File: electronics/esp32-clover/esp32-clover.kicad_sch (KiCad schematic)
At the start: 62 parts

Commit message: added pcb layout and imgs folder
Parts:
- removed J?: FTDI_CONN, symbol Connector:Conn_01x03_Male
- removed JP? (x2): SJ_B, symbol Jumper:SolderJumper_2_Bridged
- added D6: LED, LED_SMD:LED_0603_1608Metric, symbol Device:LED
- added J3: Conn_01x08_Male, Connector_PinHeader_2.54mm:PinHeader_1x08_P2.54mm_Vertical, symbol Connector:Conn_01x08_Male
- added J5: Conn_01x10_Male, Connector_PinHeader_2.54mm:PinHeader_1x10_P2.54mm_Vertical, symbol Connector:Conn_01x10_Male
- added R19: 10K, Resistor_SMD:R_0603_1608Metric, symbol Device:R
- added R20: 470, Resistor_SMD:R_0603_1608Metric, symbol Device:R
- added SW3: PROG_BTN, MCIPTG23K-V:MCIPTG23K-V, symbol MCIPTG23K-V:MCIPTG23K-V
- C1, C10, C11, C12, C13, C14, C15, C16, C17, C2, C3, C4, C5, C6, C7, C8, C9: renamed from C?; footprint Capacitor_SMD:C_0805_2012Metric -> Capacitor_SMD:C_0603_1608Metric
- D1, D3, D4, D5: renamed from D?; footprint LED_SMD:LED_0805_2012Metric -> LED_SMD:LED_0603_1608Metric
- J1: renamed from J?; footprint GCT_USB4055-30-A -> USB4055-30-A:USB4055-30-A
- J2: renamed from J?; footprint JST_S2B-PH-K-S(LF)(SN) -> S2B-PH-K-S_LF__SN:S2B-PH-K-S_LF__SN
- J4: renamed from J?; footprint (none) -> jtag:3221-10-0100-00
- JP1, JP2, JP3, JP4: renamed from JP?; footprint (none) -> Jumper:SolderJumper-2_P1.3mm_Bridged_Pad1.0x1.5mm
- LS1: renamed from LS?; footprint SPKR_PKMCS0909E4000-R1 -> PKMCS0909E4000-R1:PKMCS0909E4000-R1
- R1, R10, R11, R12, R13, R14, R15, R16, R17, R18, R2, R3, R4, R5, R6, R7, R8, R9: renamed from R?; footprint Resistor_SMD:R_0805_2012Metric -> Resistor_SMD:R_0603_1608Metric
- SW1, SW2: renamed from SW?; footprint MCIPTG23K-V_MTC -> MCIPTG23K-V:MCIPTG23K-V
- U2: renamed from U?; footprint Package_DFN_QFN:SiliconLabs_QFN-20-1EP_3x3mm_P0.5mm -> Package_DFN_QFN:SiliconLabs_QFN-20-1EP_3x3mm_P0.5mm_EP1.8x1.8mm
- U4: renamed from U?; footprint XCVR_ESP32-WROOM-32E_(16MB) -> ESP32:ESP32-WROOM-32E__16MB
- U5: renamed from U?; footprint (none) -> Package_SO:TSSOP-16_4.4x5mm_P0.65mm
- U6: renamed from U?; footprint SOP50P490X110-10N -> ADC124S101CIMM:ADC124S101CIMM
- U7: renamed from U?; footprint SOT95P280X145-6N -> DAC5571IDBVR:SOT95P280X145-6N
- Y1: renamed from Y?; footprint XTAL320X150X90 -> 32_768kHZ:ABS07AIG-32.768KHZ-T
- gave numbers to parts that had none: 4
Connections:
- net +3.3V: now also LS1.1, R18.2, R19.2
- net ADC_IN1: now also J3.2 (Pin_2)
- net ADC_IN3: now also J5.3 (Pin_3)
- net DAC_VOUT: now also J3.1 (Pin_1)
- net GND: now also D6.1 (K), J5.2 (Pin_2), SW3.4, SW3.5
- net GPIO17: now also J5.4 (Pin_4)
- net GPIO21/TCA9534_INT: now also J5.8 (Pin_8)
- net GPIO27/PIEZO: now also R17.2
- net I2C_SCL: now also J3.5 (Pin_5)
- net I2C_SDA: now also J3.6 (Pin_6)
- net SPI_MISO: now also J5.7 (Pin_7)
- net SPI_MOSI: now also J5.6 (Pin_6)
- net SPI_SCK: now also J5.5 (Pin_5)
- net TCA9534_P2: now also J3.4 (Pin_4)
- net TCA9534_P3: now also J3.3 (Pin_3)
- net UART_RX: now also J5.10 (Pin_10)
- net UART_RX1: now also J3.7 (Pin_7)
- net UART_TX: now also J5.9 (Pin_9)
- net UART_TX1: now also J3.8 (Pin_8)
- net VBAT: now also J5.1 (Pin_1)
- net VBUS: now also R20.2
- net GPI34 renamed GPI34/BTN
- net GPI34/BTN: now also R19.1, SW3.1
- new net: D6.2 (A), R20.1
- no-connect marks 27 -> 29
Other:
- note added: "TODO ADD UART TO EXTERNAL PINS"
- note removed: "UART Pins"

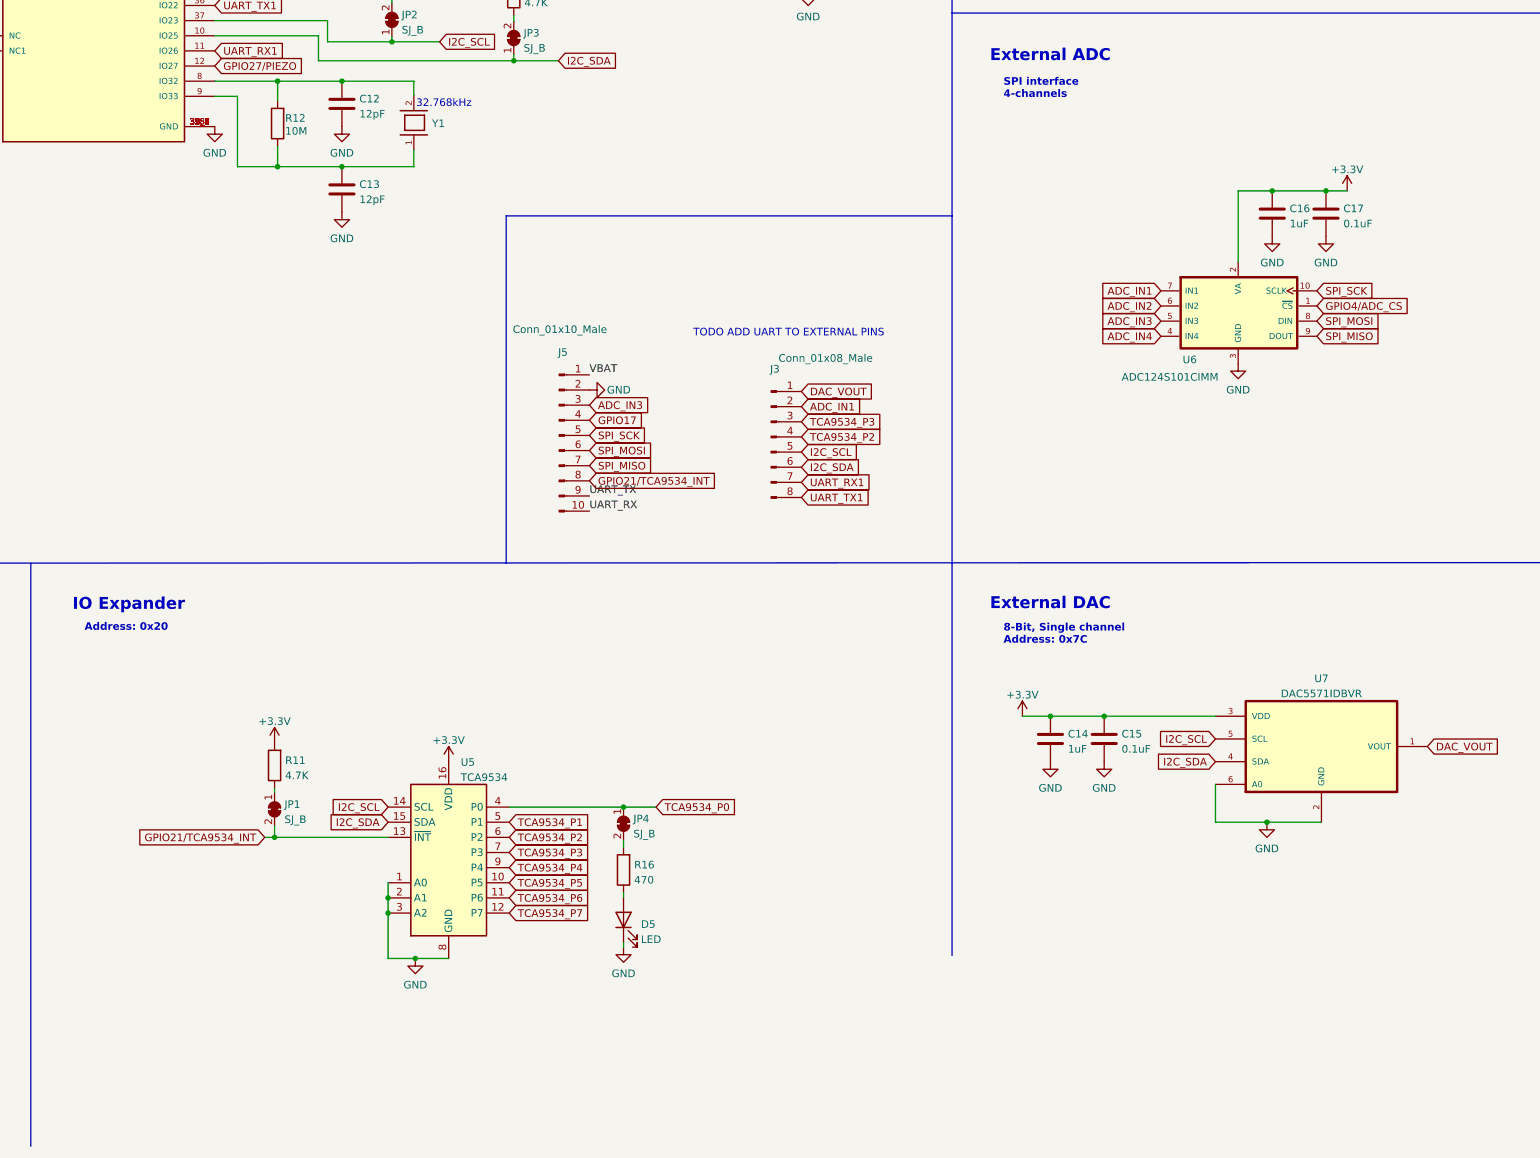
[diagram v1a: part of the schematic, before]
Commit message: added arduino variant pin definitions, still more to do
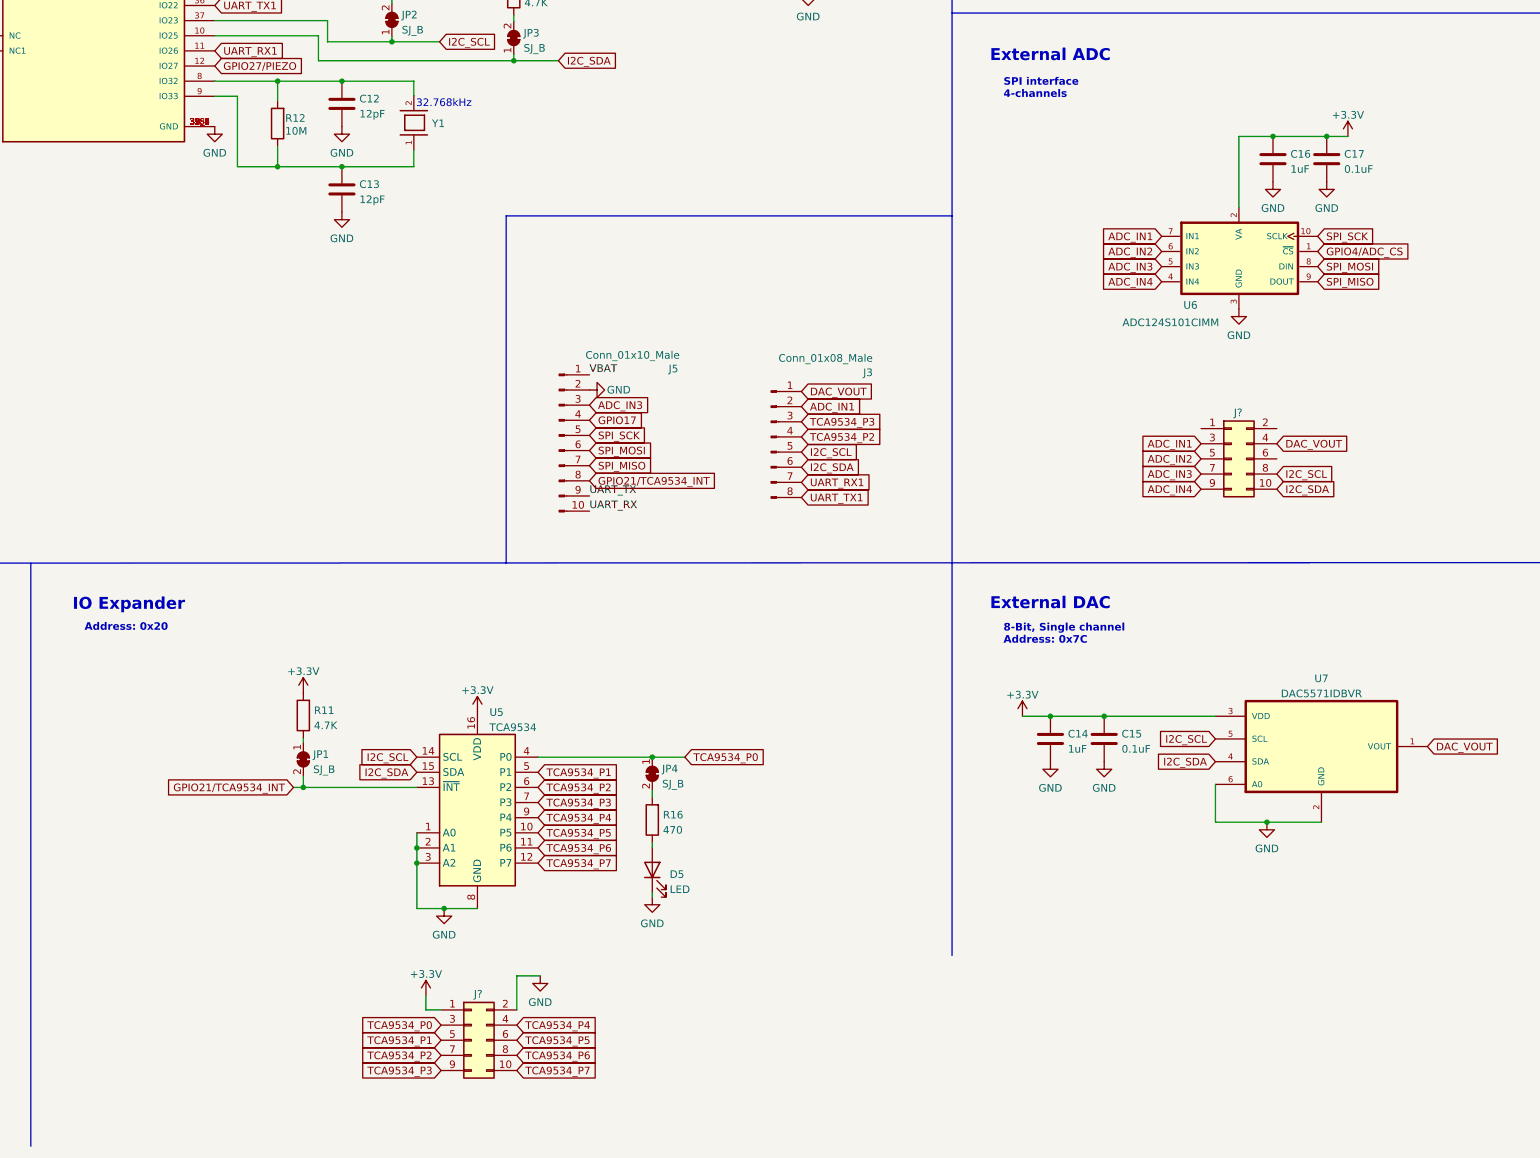
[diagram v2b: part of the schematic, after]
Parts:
- added J? (x2): Conn_02x05_Odd_Even, symbol Connector_Generic:Conn_02x05_Odd_Even
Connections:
- net +3.3V: now also J?.1 (Pin_1)
- net ADC_IN1: now also J?.3 (Pin_3)
- net ADC_IN2: now also J?.5 (Pin_5)
- net ADC_IN3: now also J?.7 (Pin_7)
- net ADC_IN4: now also J?.9 (Pin_9)
- net DAC_VOUT: now also J?.4 (Pin_4)
- net GND: now also J?.2 (Pin_2)
- net I2C_SCL: now also J?.8 (Pin_8)
- net I2C_SDA: now also J?.10 (Pin_10)
- net TCA9534_P0: now also J?.3 (Pin_3)
- net TCA9534_P1: now also J?.5 (Pin_5)
- net TCA9534_P2: now also J?.7 (Pin_7)
- net TCA9534_P3: now also J?.9 (Pin_9)
- net TCA9534_P4: now also J?.4 (Pin_4)
- net TCA9534_P5: now also J?.6 (Pin_6)
- net TCA9534_P6: now also J?.8 (Pin_8)
- net TCA9534_P7: now also J?.10 (Pin_10)
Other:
- note removed: "TODO ADD UART TO EXTERNAL PINS"
- moved on the sheet: C16, C17, D5, JP1, JP4, R11, R16, U5, U6

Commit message: update for v0.2
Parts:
- removed JP1, JP2, JP3, JP4: SJ_B, Jumper:SolderJumper-2_P1.3mm_Bridged_Pad1.0x1.5mm, symbol Jumper:SolderJumper_2_Bridged
- added C18: 4.7uF, Capacitor_SMD:C_0603_1608Metric, symbol Device:C
- added C19: TBD, Capacitor_SMD:C_0603_1608Metric, symbol Device:C
- added D7: D_Schottky, symbol Device:D_Schottky
- added Q2: MMDT3904, Package_TO_SOT_SMD:SOT-363_SC-70-6, symbol Transistor_BJT:MMDT3904
- added Q3: DMG2305UX-13, SOT91P240X110-3N, symbol DMG2305UX-13:DMG2305UX-13
- added R21: 1M, Resistor_SMD:R_0603_1608Metric, symbol Device:R
- added R22, R23: 10K, Resistor_SMD:R_0603_1608Metric, symbol Device:R
- added R24: 100K, Resistor_SMD:R_0603_1608Metric, symbol Device:R
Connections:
- net +3.3V: no longer U6.2 (VA)
- net ESP32_BOOT: now also Q2.3 (C2)
- net GND: now also C18.2, C19.2, R21.1, R24.1; no longer J1.S1 (SHIELD), J1.S2 (SHIELD), J1.S3 (SHIELD), J1.S4 (SHIELD), U6.3 (GND)
- net GPIO21/TCA9534_INT: now also R11.1
- net GPIO4/ADC_CS: no longer U6.1 (~{CS})
- net I2C_SCL: now also R14.1
- net I2C_SDA: now also R15.1
- net SPI_MISO: no longer U6.9 (DOUT)
- net SPI_MOSI: no longer U6.8 (DIN)
- net SPI_SCK: no longer U6.10 (SCLK)
- net TCA9534_P0: now also R16.2
- net USB_D+: now also J1.B6 (DP2)
- net USB_D-: now also J1.B7 (DN2)
- net VBUS: now also D7.2 (A), Q3.1, R24.2
- net at C12.1, R12.2, U4.8 (IO32): no longer Y1.2
- net at Q1.3 (C), R18.1: no longer LS1.2
- net ESP_EN: now reaches C9.1, R10.1, SW1.1, U4.3 (EN)
- net ESP_EN: now also Q2.6 (C1)
- net UART_DTR: now reaches U2.15 (~{CTS})
- net UART_DTR: now also Q2.4 (E2), R22.2
- net UART_RTS: now reaches U2.16 (~{RTS})
- net UART_RTS: now also Q2.1 (E1), R23.2
- net VBAT renamed +BATT
- net +BATT: now also Q3.3; no longer C5.1, U3.1 (VIN), U3.3 (EN)
- new net: C18.1, J1.S1 (SHIELD), J1.S2 (SHIELD), J1.S3 (SHIELD), J1.S4 (SHIELD), R21.2
- new net: Q2.2 (B1), R22.1
- new net: C19.1, C5.1, D7.1 (K), Q3.2, U3.1 (VIN), U3.3 (EN)
- new net: Q2.5 (B2), R23.1
- no-connect marks 29 -> 25
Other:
- note added: "3V3 Regulator"
- note added: "Battery Charger"
- note added: "Pwr"
- note added: "Single cell LiPo Charge Current: 400 mA Float voltage: 4.2 V Note: Max 500 mA with 2K resistor on PROG)"
- note added: "Upto 4 kHz (65 dB)"
- note added: "When VBUS (USB) is connected system is powered by USB."
- note removed: "Battery Charger & 3.3V Regulator"
- note removed: "Single cell LiPo Charge Current: 400 mA (Max 500 mA with 2K resistor on PROG) Float voltage: 4.2 V"
- note removed: "Upto 4 kHz (65 dB) Disable by cutting both jumpers"
- moved on the sheet: C1, C14, C15, C16, C17, C4, C5, C8, D1, D5, J2, J?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

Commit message: update for v2
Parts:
- removed C1, C18, C2, C4, C7: 4.7uF, Capacitor_SMD:C_0603_1608Metric, symbol Device:C
- removed C14, C16, C5, C8: 1uF, Capacitor_SMD:C_0603_1608Metric, symbol Device:C
- removed C15, C17, C3, C6: 0.1uF, Capacitor_SMD:C_0603_1608Metric, symbol Device:C
- removed C19: TBD, Capacitor_SMD:C_0603_1608Metric, symbol Device:C
- removed D1, D3, D4, D5, D6: LED, LED_SMD:LED_0603_1608Metric, symbol Device:LED
- removed D2: SP0503BAHT, Package_TO_SOT_SMD:SOT-143, symbol Power_Protection:SP0503BAHT
- removed D7: D_Schottky, symbol Device:D_Schottky
- removed J1: USB4055-30-A, USB4055-30-A:USB4055-30-A, symbol USB4055-30-A:USB4055-30-A
- removed J2: BATT_CONN, S2B-PH-K-S_LF__SN:S2B-PH-K-S_LF__SN, symbol S2B-PH-K-S_LF__SN:S2B-PH-K-S(LF)(SN)
- removed J3: Conn_01x08_Male, Connector_PinHeader_2.54mm:PinHeader_1x08_P2.54mm_Vertical, symbol Connector:Conn_01x08_Male
- removed J5: Conn_01x10_Male, Connector_PinHeader_2.54mm:PinHeader_1x10_P2.54mm_Vertical, symbol Connector:Conn_01x10_Male
- removed J? (x2): Conn_02x05_Odd_Even, symbol Connector_Generic:Conn_02x05_Odd_Even
- removed Q2: MMDT3904, Package_TO_SOT_SMD:SOT-363_SC-70-6, symbol Transistor_BJT:MMDT3904
- removed Q3: DMG2305UX-13, SOT91P240X110-3N, symbol DMG2305UX-13:DMG2305UX-13
- removed R1, R7: 5.1K, Resistor_SMD:R_0603_1608Metric, symbol Device:R
- removed R11: 4.7K, Resistor_SMD:R_0603_1608Metric, symbol Device:R
- removed R16, R2, R20: 470, Resistor_SMD:R_0603_1608Metric, symbol Device:R
- removed R21: 1M, Resistor_SMD:R_0603_1608Metric, symbol Device:R
- removed R22, R23: 10K, Resistor_SMD:R_0603_1608Metric, symbol Device:R
- removed R24: 100K, Resistor_SMD:R_0603_1608Metric, symbol Device:R
- removed R3: 2.5K, Resistor_SMD:R_0603_1608Metric, symbol Device:R
- removed R4: 22.1K, Resistor_SMD:R_0603_1608Metric, symbol Device:R
- removed R5: 47.5K, Resistor_SMD:R_0603_1608Metric, symbol Device:R
- removed R6, R8, R9: 1K, Resistor_SMD:R_0603_1608Metric, symbol Device:R
- removed SW1: RESET, MCIPTG23K-V:MCIPTG23K-V, symbol MCIPTG23K-V:MCIPTG23K-V
- removed SW2: BOOT, MCIPTG23K-V:MCIPTG23K-V, symbol MCIPTG23K-V:MCIPTG23K-V
- removed SW3: PROG_BTN, MCIPTG23K-V:MCIPTG23K-V, symbol MCIPTG23K-V:MCIPTG23K-V
- removed U1: MCP73832-2-OT, Package_TO_SOT_SMD:SOT-23-5, symbol Battery_Management:MCP73832-2-OT
- removed U2: CP2102N-Axx-xQFN20, Package_DFN_QFN:SiliconLabs_QFN-20-1EP_3x3mm_P0.5mm_EP1.8x1.8mm, symbol Interface_USB:CP2102N-Axx-xQFN20
- removed U3: NCP163ASN330T1G, Package_TO_SOT_SMD:SOT-23-5, symbol Regulator_Linear:NCP163ASN330T1G
- removed U5: TCA9534, Package_SO:TSSOP-16_4.4x5mm_P0.65mm, symbol Interface_Expansion:TCA9534
- removed U6: ADC124S101CIMM, ADC124S101CIMM:ADC124S101CIMM, symbol ADC124S101CIMM:ADC124S101CIMM
- removed U7: DAC5571IDBVR, DAC5571IDBVR:SOT95P280X145-6N, symbol DAC5571IDBVR:DAC5571IDBVR
- added D10, D8, D9: SP4020-01FTG, SOD2613X114N, symbol SP4020-01FTG:SP4020-01FTG
- added J5, J8, J9: TBP02R2-381-05BE, CUI_TBP02R2-381-05BE, symbol TBP02R2-381-05BE:TBP02R2-381-05BE
- added S1, S2, S3: TL1105F160Q, SW_TL1105F160Q, symbol TL1105F160Q:TL1105F160Q
- LS1: footprint PKMCS0909E4000-R1:PKMCS0909E4000-R1 -> SPKR_PKMCS0909E4000-R1
- Y1: footprint 32_768kHZ:ABS07AIG-32.768KHZ-T -> XTAL320X150X90
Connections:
- net +3.3V: now also J9.2
- net +BATT: now also J9.3
- net ESP32_BOOT: now also D10.1 (K), S3.1
- net ESP_EN: now also D8.1 (K), J9.4, S1.3
- net GND: now also D10.2 (A), D8.2 (A), D9.2 (A), J9.5, S1.2, S2.2, S3.4
- net GPI34/BTN: now also D9.1 (K), S2.3
- net GPIO17: now also J8.5
- net GPIO21/TCA9534_INT: now also J5.4
- net I2C_SCL: now also J8.4
- net I2C_SDA: now also J8.3
- net SPI_MISO: now also J5.2
- net SPI_MOSI: now also J5.3
- net SPI_SCK: now also J5.1
- net UART_RX1: now also J8.2
- net UART_TX1: now also J8.1
- net VBUS: now also J9.1
- net at Y1.2: now also C12.1, R12.2, U4.8 (IO32)
- net at Q1.3 (C), R18.1: now also LS1.2
- net GPI36 renamed ADC_LDAC
- net GPI39 renamed ADC_RDY/BSY
- net GPIO27/PIEZO renamed GPIO27
- net GPIO27: now also J5.5; no longer R17.2
- net GPIO4/ADC_CS renamed GPIO4
- new net dac/DAC_VOUTA: R17.2
- no-connect marks 25 -> 8
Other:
- added sheet adc (adc.kicad_sch)
- added sheet can (can.kicad_sch)
- added sheet dac (dac.kicad_sch)
- added sheet gpio (gpio.kicad_sch)
- added sheet pwr (pwr.kicad_sch)
- added sheet sd (sd.kicad_sch)
- added sheet usb (usb.kicad_sch)
- note added: "ADC"
- note added: "CAN"
- note added: "DAC"
- note added: "ESP32"
- note added: "GPIO"
- note added: "POWER"
- note added: "Prog"
- note added: "Reset"
- note added: "SD-CARD"
- note added: "USB"
- note removed: "3V3 Regulator"
- note removed: "8-Bit, Single channel Address: 0x7C"
- note removed: "Address: 0x20"
- note removed: "Battery Charger"
- note removed: "ESD-Protection"
- note removed: "External ADC"
- note removed: "External DAC"
- note removed: "IO Expander"
- note removed: "Pwr"
- note removed: "SPI interface 4-channels"
- note removed: "Single cell LiPo Charge Current: 400 mA Float voltage: 4.2 V Note: Max 500 mA with 2K resistor on PROG)"
- note removed: "USB-C, USB to UART and ESP32"
- note removed: "When VBUS (USB) is connected system is powered by USB."
- moved on the sheet: C10, C11, C12, C13, C9, J4, LS1, Q1, R10, R12, R13, R14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

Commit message: update before switching to stm32
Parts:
- removed J5, J8, J9: TBP02R2-381-05BE, CUI_TBP02R2-381-05BE, symbol TBP02R2-381-05BE:TBP02R2-381-05BE
- removed LS1: PKMCS0909E4000-R1, SPKR_PKMCS0909E4000-R1, symbol PKMCS0909E4000-R1:PKMCS0909E4000-R1
- removed S1, S2, S3: TL1105F160Q, SW_TL1105F160Q, symbol TL1105F160Q:TL1105F160Q
- removed U4: ESP32-WROOM-32E_(16MB), ESP32:ESP32-WROOM-32E__16MB, symbol ESP32-WROOM-32E__16MB:ESP32-WROOM-32E_(16MB)
- removed Y1: ABS07AIG-32.768KHZ-T, XTAL320X150X90, symbol ABS07AIG-32.768KHZ-T:ABS07AIG-32.768KHZ-T
- added D? (x2): ESDA6V1BC6, Package_TO_SOT_SMD:SOT-23-6, symbol Power_Protection:ESDA6V1BC6
- added J? (x4): TBP02R2-381-05BE, connectors:TBP02R2-381-05BE, symbol connectors:TBP02R2-381-05BE
- added LS?: PKMCS0909E4000-R1, piezo_buzzers:PKMCS0909E4000-R1, symbol piezo_buzzers:PKMCS0909E4000-R1
- added S? (x3): TL1105F160Q, buttons:TL1105F160Q, symbol buttons:TL1105F160Q
- added U?: ESP32-WROOM-32E_(16MB), microcontrollers:ESP32-WROOM-32E_16MB, symbol microcontrollers:ESP32-WROOM-32E_(16MB)
- added Y?: ABS07AIG-32.768KHZ-T, crystals:ABS07AIG-32.768KHZ-T, symbol crystals:ABS07AIG-32.768KHZ-T
- D1: renamed from D9; footprint SOD2613X114N -> SP4020-01FTG:SOD2613X114N
- D2: renamed from D8; footprint SOD2613X114N -> SP4020-01FTG:SOD2613X114N
- D3: renamed from D10; footprint SOD2613X114N -> SP4020-01FTG:SOD2613X114N
- renumbered C9 to C1, C10 to C2, C11 to C3, C12 to C4, C13 to C5, J4 to J5, R19 to R1, R10 to R2, R12 to R3, R13 to R4, R14 to R5, R15 to R6, R17 to R7, R18 to R8
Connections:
- net +3.3V: now also J?.2, LS?.1, U?.2 (3V3)
- net +BATT: now also J?.3
- net DEBUG_TCK: now also U?.16 (IO13)
- net DEBUG_TDI: now also U?.14 (IO12)
- net DEBUG_TDO: now also U?.23 (IO15)
- net DEBUG_TMS: now also U?.13 (IO14)
- net ESP32_BOOT: now also S?.1, U?.25 (IO0)
- net ESP_EN: now also J?.4, S?.3, U?.3 (EN)
- net GND: now also D?.2 (COM), D?.2 (COM), D?.5 (COM), D?.5 (COM), J?.5, J?.5, S?.2, S?.2, S?.4, U?.1 (GND), U?.15 (GND), U?.38 (GND), U?.39_1 (GND), U?.39_2 (GND), U?.39_3 (GND), U?.39_4 (GND), U?.39_5 (GND), U?.39_6 (GND), U?.39_7 (GND), U?.39_8 (GND), U?.39_9 (GND)
- net GPI34/BTN: now also S?.3, U?.6 (IO34)
- net GPI35: now also J?.5, U?.7 (IO35)
- net GPIO17: now also J?.2, U?.28 (IO17)
- net GPIO4: now also J?.1, U?.26 (IO4)
- net I2C_SCL: now also D?.4 (TVS3), J?.5, U?.37 (IO23)
- net I2C_SDA: now also D?.3 (TVS2), J?.4, U?.10 (IO25)
- net SPI_MISO: now also D?.3 (TVS2), J?.2, U?.31 (IO19)
- net SPI_MOSI: now also D?.4 (TVS3), J?.3, U?.30 (IO18)
- net SPI_SCK: now also D?.1 (TVS1), J?.1, U?.29 (IO5)
- net UART_RX: now also J?.2, U?.35 (TXD0)
- net UART_RX1: now also D?.1 (TVS1), J?.4, U?.11 (IO26)
- net UART_TX: now also J?.1, U?.34 (RXD0)
- net UART_TX1: now also D?.6 (TVS4), J?.3, U?.36 (IO22)
- net VBUS: now also J?.1
- net at C5.1, R3.1: now also U?.9 (IO33), Y?.1
- net at C4.1, R3.2: now also U?.8 (IO32), Y?.2
- net at Q1.3 (C), R8.1: now also LS?.2
- net at R4.1: now also U?.27 (IO16)
- new net: U?.17 (NC), U?.18 (NC), U?.19 (NC), U?.20 (NC), U?.21 (NC), U?.22 (NC)
- new net DAC_RDY/BSY: U?.5 (SENSOR_VN)
- new net GPIO21/GPIO1_INT: J?.3, U?.33 (IO21)
- new net GPIO27/GPIO2_INT: J?.4, U?.12 (IO27)
- no-connect marks 8 -> 9
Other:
- added sheet reg (reg.kicad_sch)
- sheet adc ports: added ADC_CS; removed GPIO4/ADC_CS
- sheet dac ports: added DAC_LDAC, DAC_RDY/BSY; removed ADC_LDAC, ADC_RDY/BSY
- sheet gpio ports: added GPIO1_P7/PV_RST, GPIO2_INT, GPIO2_P1/DAC_LDAC; removed GPIO1_P7
- sheet pwr ports: added PV_RESET; removed 5V_EN
- note added: "Boot"
- note added: "Regulation"
- moved on the sheet: C1, C2, C3, C4, C5, D1, D2, D3, J5, Q1, R1, R2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
